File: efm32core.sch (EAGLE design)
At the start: 66 parts, among them Q1 MMBT5088, U3 USD-SOCKETNEW, X1 48.0MHz, Y1 32.768kHz

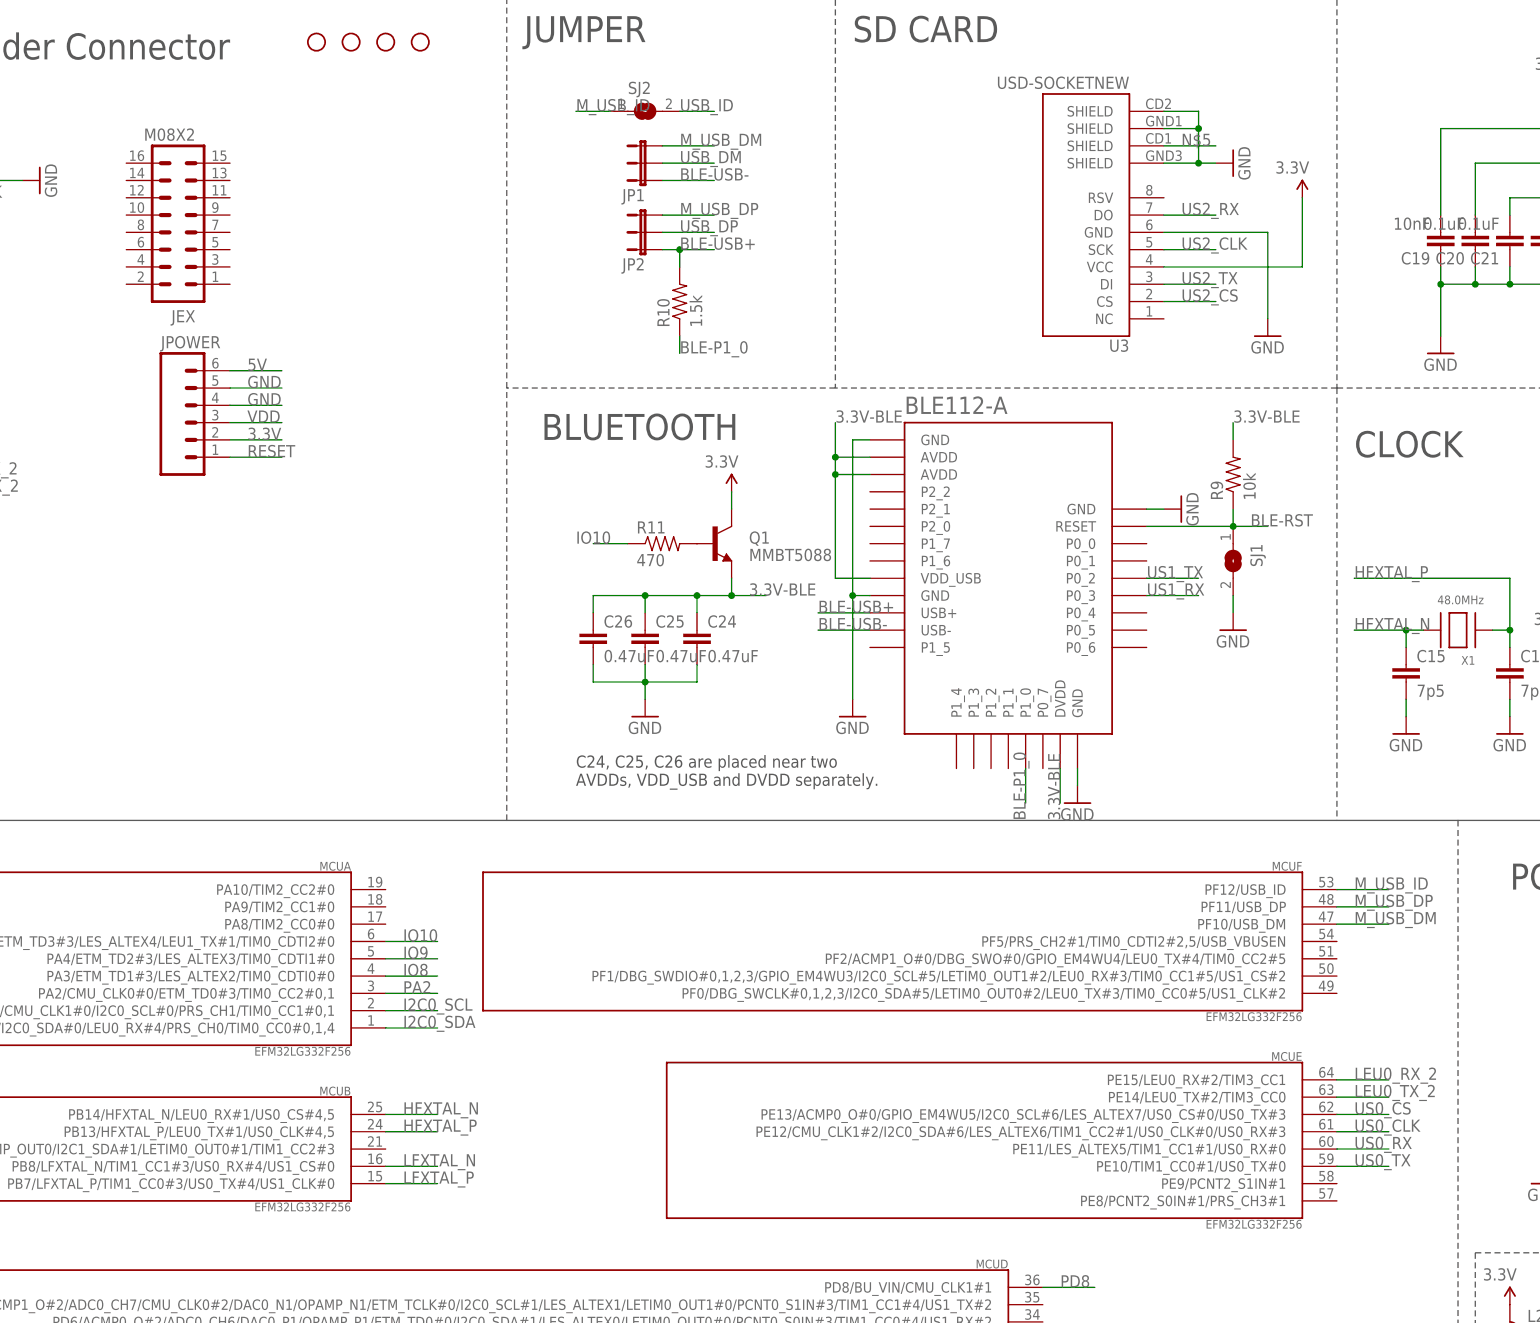
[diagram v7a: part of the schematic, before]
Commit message: update swd wires
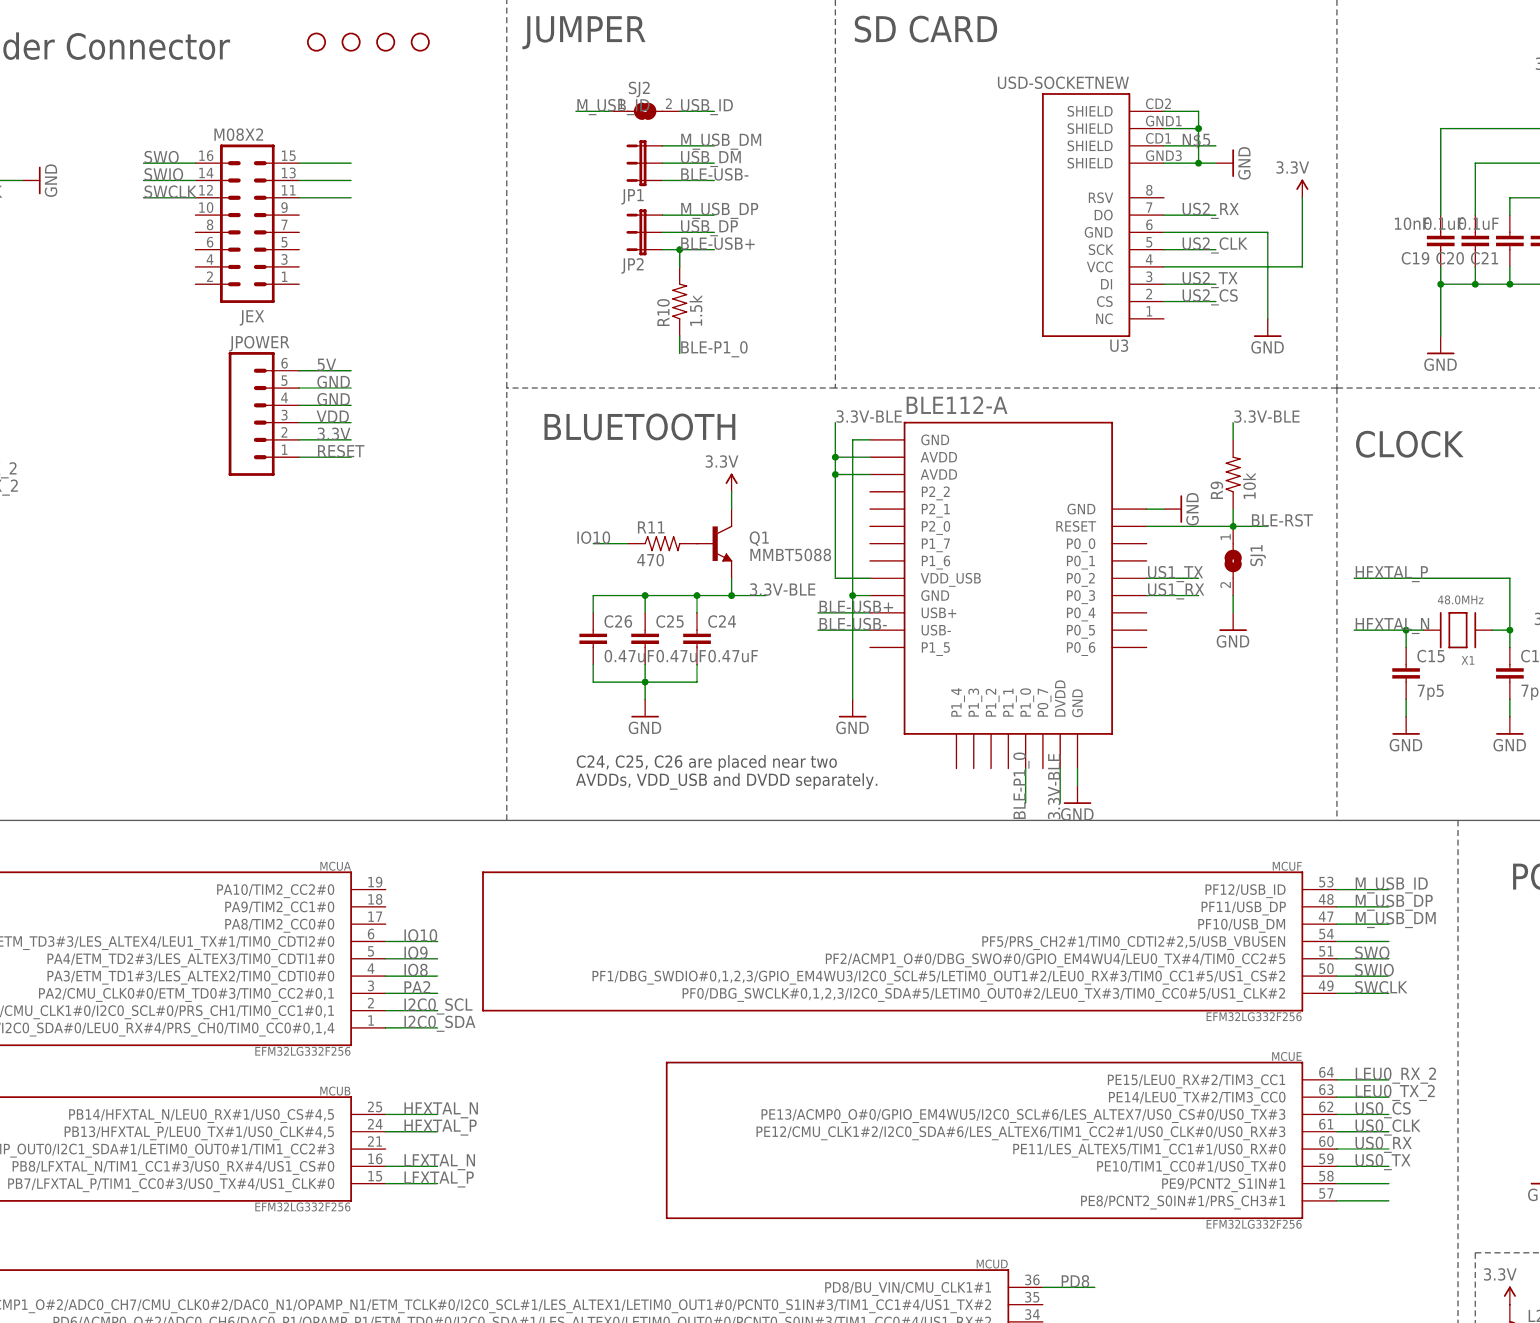
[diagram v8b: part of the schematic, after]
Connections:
- new net N$10: MCUF.PF5/PRS_CH2#1/TIM0_CDTI2#2,5/USB_VBUSEN
- new net N$11: MCUE.PE8/PCNT2_S0IN#1/PRS_CH3#1
- new net N$16: MCUE.PE9/PCNT2_S1IN#1
- new net N$17: JEX.11
- new net N$18: JEX.13
- new net N$20: JEX.15
- new net SWCLK: JEX.12, MCUF.PF0/DBG_SWCLK#0,1,2,3/I2C0_SDA#5/LETIM0_OUT0#2/LEU0_TX#3/TIM0_CC0#5/US1_CLK#2
- new net SWIO: JEX.14, MCUF.PF1/DBG_SWDIO#0,1,2,3/GPIO_EM4WU3/I2C0_SCL#5/LETIM0_OUT1#2/LEU0_RX#3/TIM0_CC1#5/US1_CS#2
- new net SWO: JEX.16, MCUF.PF2/ACMP1_O#0/DBG_SWO#0/GPIO_EM4WU4/LEU0_TX#4/TIM0_CC2#5
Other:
- moved on the sheet: JEX, JPOWER
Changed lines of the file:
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@@
 <instance part="JIOL" gate="G$1" x="27.94" y="190.5"/>
 <instance part="JAD" gate="G$1" x="27.94" y="157.48"/>
-<instance part="JPOWER" gate="G$1" x="73.66" y="193.04"/>
-<instance part="JEX" gate="G$1" x="71.12" y="223.52" rot="R180"/>
+<instance part="JPOWER" gate="G$1" x="83.82" y="193.04"/>
+<instance part="JEX" gate="G$1" x="81.28" y="223.52" rot="R180"/>
 <instance part="FRAME1" gate="G$1" x="0" y="0"/>
 <instance part="PMIC1" gate="G$1" x="350.52" y="109.22" rot="MR0"/>
@@
 <segment>
 <pinref part="JPOWER" gate="G$1" pin="2"/>
-<wire x1="78.74" y1="190.5" x2="86.36" y2="190.5" width="0.1524" layer="91"/>
-<label x="81.28" y="190.5" size="1.778" layer="95"/>
+<wire x1="88.9" y1="190.5" x2="96.52" y2="190.5" width="0.1524" layer="91"/>
+<label x="91.44" y="190.5" size="1.778" layer="95"/>
 </segment>
 <segment>
@@
 <segment>
 <pinref part="JPOWER" gate="G$1" pin="3"/>
-<wire x1="78.74" y1="193.04" x2="86.36" y2="193.04" width="0.1524" layer="91"/>
-<label x="81.28" y="193.04" size="1.778" layer="95"/>
+<wire x1="88.9" y1="193.04" x2="96.52" y2="193.04" width="0.1524" layer="91"/>
+<label x="91.44" y="193.04" size="1.778" layer="95"/>
 </segment>
 <segment>
@@
 <segment>
 <pinref part="JPOWER" gate="G$1" pin="5"/>
-<wire x1="78.74" y1="198.12" x2="86.36" y2="198.12" width="0.1524" layer="91"/>
-<label x="81.28" y="198.12" size="1.778" layer="95"/>
+<wire x1="88.9" y1="198.12" x2="96.52" y2="198.12" width="0.1524" layer="91"/>
+<label x="91.44" y="198.12" size="1.778" layer="95"/>
 </segment>
 <segment>
 <pinref part="JPOWER" gate="G$1" pin="4"/>
-<wire x1="78.74" y1="195.58" x2="86.36" y2="195.58" width="0.1524" layer="91"/>
-<label x="81.28" y="195.58" size="1.778" layer="95"/>
+<wire x1="88.9" y1="195.58" x2="96.52" y2="195.58" width="0.1524" layer="91"/>
+<label x="91.44" y="195.58" size="1.778" layer="95"/>
 </segment>
 <segment>
@@
 <segment>
 <pinref part="JPOWER" gate="G$1" pin="6"/>
-<wire x1="78.74" y1="200.66" x2="86.36" y2="200.66" width="0.1524" layer="91"/>
-<label x="81.28" y="200.66" size="1.778" layer="95"/>
+<wire x1="88.9" y1="200.66" x2="96.52" y2="200.66" width="0.1524" layer="91"/>
+<label x="91.44" y="200.66" size="1.778" layer="95"/>
 </segment>
 </net>
@@
 <segment>
 <pinref part="JPOWER" gate="G$1" pin="1"/>
-<wire x1="78.74" y1="187.96" x2="86.36" y2="187.96" width="0.1524" layer="91"/>
-<label x="81.28" y="187.96" size="1.778" layer="95"/>
+<wire x1="88.9" y1="187.96" x2="96.52" y2="187.96" width="0.1524" layer="91"/>
+<label x="91.44" y="187.96" size="1.778" layer="95"/>
 </segment>
 </net>
@@
 </segment>
 </net>
+<net name="N$10" class="0">
+<segment>
+<pinref part="MCU" gate="F" pin="PF5/PRS_CH2#1/TIM0_CDTI2#2,5/USB_VBUSEN"/>
+<wire x1="241.3" y1="116.84" x2="248.92" y2="116.84" width="0.1524" layer="91"/>
+</segment>
+</net>
+<net name="N$11" class="0">
+<segment>
+<pinref part="MCU" gate="E" pin="PE8/PCNT2_S0IN#1/PRS_CH3#1"/>
+<wire x1="241.3" y1="78.74" x2="248.92" y2="78.74" width="0.1524" layer="91"/>
+</segment>
+</net>
+<net name="N$16" class="0">
+<segment>
+<pinref part="MCU" gate="E" pin="PE9/PCNT2_S1IN#1"/>
+<wire x1="241.3" y1="81.28" x2="248.92" y2="81.28" width="0.1524" layer="91"/>
+</segment>
+</net>
+<net name="N$17" class="0">
+<segment>
+<pinref part="JEX" gate="G$1" pin="11"/>
+<wire x1="88.9" y1="226.06" x2="96.52" y2="226.06" width="0.1524" layer="91"/>
+</segment>
+</net>
+<net name="N$18" class="0">
+<segment>
+<pinref part="JEX" gate="G$1" pin="13"/>
+<wire x1="88.9" y1="228.6" x2="96.52" y2="228.6" width="0.1524" layer="91"/>
+</segment>
+</net>
+<net name="N$20" class="0">
+<segment>
+<pinref part="JEX" gate="G$1" pin="15"/>
+<wire x1="88.9" y1="231.14" x2="96.52" y2="231.14" width="0.1524" layer="91"/>
+</segment>
+</net>
+<net name="SWIO" class="0">
+<segment>
+<pinref part="JEX" gate="G$1" pin="14"/>
+<wire x1="73.66" y1="228.6" x2="66.04" y2="228.6" width="0.1524" layer="91"/>
+<label x="66.04" y="228.6" size="1.778" layer="95"/>
+</segment>
+<segment>
+<pinref part="MCU" gate="F" pin="PF1/DBG_SWDIO#0,1,2,3/GPIO_EM4WU3/I2C0_SCL#5/LETIM0_OUT1#2/LEU0_RX#3/TIM0_CC1#5/US1_CS#2"/>
+<wire x1="241.3" y1="111.76" x2="248.92" y2="111.76" width="0.1524" layer="91"/>
+<label x="243.84" y="111.76" size="1.778" layer="95"/>
+</segment>
+</net>
+<net name="SWO" class="0">
+<segment>
+<pinref part="JEX" gate="G$1" pin="16"/>
+<wire x1="73.66" y1="231.14" x2="66.04" y2="231.14" width="0.1524" layer="91"/>
+<label x="66.04" y="231.14" size="1.778" layer="95"/>
+</segment>
+<segment>
+<pinref part="MCU" gate="F" pin="PF2/ACMP1_O#0/DBG_SWO#0/GPIO_EM4WU4/LEU0_TX#4/TIM0_CC2#5"/>
+<wire x1="241.3" y1="114.3" x2="248.92" y2="114.3" width="0.1524" layer="91"/>
+<label x="243.84" y="114.3" size="1.778" layer="95"/>
+</segment>
+</net>
+<net name="SWCLK" class="0">
+<segment>
+<pinref part="JEX" gate="G$1" pin="12"/>
+<wire x1="73.66" y1="226.06" x2="66.04" y2="226.06" width="0.1524" layer="91"/>
+<label x="66.04" y="226.06" size="1.778" layer="95"/>
+</segment>
+<segment>
+<pinref part="MCU" gate="F" pin="PF0/DBG_SWCLK#0,1,2,3/I2C0_SDA#5/LETIM0_OUT0#2/LEU0_TX#3/TIM0_CC0#5/US1_CLK#2"/>
+<wire x1="241.3" y1="109.22" x2="248.92" y2="109.22" width="0.1524" layer="91"/>
+<label x="243.84" y="109.22" size="1.778" layer="95"/>
+</segment>
+</net>
